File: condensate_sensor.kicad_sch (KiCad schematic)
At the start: 3 parts

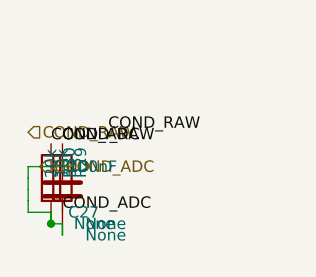
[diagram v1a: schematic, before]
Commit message: fix router map cell no more mark for pins
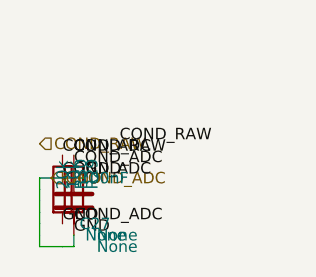
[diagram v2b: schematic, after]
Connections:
- net COND_ADC: now also C27.1

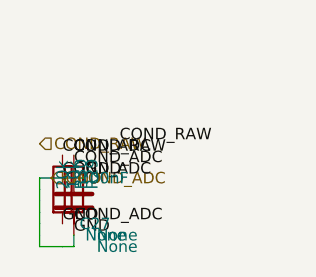
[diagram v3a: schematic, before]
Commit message: исправлены метки
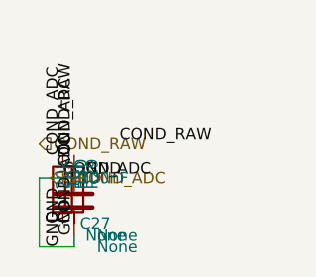
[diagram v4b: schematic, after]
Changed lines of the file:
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@@
 		(instances
 			(project "Untitled"
-				(path "/63851d28-1635-4156-be79-71811504eb15"
+				(path "/a59e5e4e-0756-472a-ad31-66ebbca15e78"
 					(reference "C27")
 					(unit 1)
@@
 		(instances
 			(project "Untitled"
-				(path "/63851d28-1635-4156-be79-71811504eb15"
+				(path "/a59e5e4e-0756-472a-ad31-66ebbca15e78"
 					(reference "R29")
 					(unit 1)
@@
 		(instances
 			(project "Untitled"
-				(path "/63851d28-1635-4156-be79-71811504eb15"
+				(path "/a59e5e4e-0756-472a-ad31-66ebbca15e78"
 					(reference "R30")
 					(unit 1)
@@
 	)
 	(label "GND"
-		(at 15.24 21.59 0)
-		(effects
-			(font
-				(size 1.27 1.27)
-			)
-			(justify left bottom)
-		)
-	)
-	(label "GND"
-		(at 16.51 22.86 0)
-		(effects
-			(font
-				(size 1.27 1.27)
-			)
-			(justify left bottom)
-		)
-	)
-	(label "GND"
-		(at 17.78 16.51 0)
+		(at 15.24 21.59 270)
+		(effects
+			(font
+				(size 1.27 1.27)
+			)
+			(justify left bottom)
+		)
+	)
+	(label "GND"
+		(at 16.51 22.86 270)
+		(effects
+			(font
+				(size 1.27 1.27)
+			)
+			(justify left bottom)
+		)
+	)
+	(label "GND"
+		(at 17.78 16.51 180)
+		(effects
+			(font
+				(size 1.27 1.27)
+			)
+			(justify left bottom)
+		)
+	)
+	(label "GND"
+		(at 15.24 24.13 270)
 		(effects
 			(font
@@
 	)
 	(label "COND_RAW"
-		(at 16.51 13.97 0)
+		(at 16.51 13.97 90)
 		(effects
 			(font
@@
 	)
 	(label "COND_RAW"
-		(at 21.59 12.7 0)
-		(effects
-			(font
-				(size 1.27 1.27)
-			)
-			(justify left bottom)
-		)
-	)
-	(label "COND_ADC"
-		(at 15.24 13.97 0)
-		(effects
-			(font
-				(size 1.27 1.27)
-			)
-			(justify left bottom)
-		)
-	)
-	(label "COND_ADC"
-		(at 16.51 15.24 0)
-		(effects
-			(font
-				(size 1.27 1.27)
-			)
-			(justify left bottom)
-		)
-	)
-	(label "COND_ADC"
-		(at 15.24 16.51 0)
-		(effects
-			(font
-				(size 1.27 1.27)
-			)
-			(justify left bottom)
-		)
-	)
-	(label "COND_ADC"
-		(at 16.51 21.59 0)
-		(effects
-			(font
+		(at 21.59 12.7 180)
+		(effects
+			(font
+				(size 1.27 1.27)
+			)
+			(justify left bottom)
+		)
+	)
+	(label "COND_ADC"
+		(at 15.24 13.97 90)
+		(effects
+			(font
+				(size 1.27 1.27)
+			)
+			(justify left bottom)
+		)
+	)
+	(label "COND_ADC"
+		(at 16.51 15.24 90)
+		(effects
+			(font
+				(size 1.27 1.27)
+			)
+			(justify left bottom)
+		)
+	)
+	(label "COND_ADC"
+		(at 15.24 16.51 0.0000)
+		(effects
+			(font
+				(size 1.27 1.27)
+			)
+			(justify left bottom)
+		)
+	)
+	(label "COND_ADC"
+		(at 16.51 21.59 270)
+		(effects
+			(font

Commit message: fix writer
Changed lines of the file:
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@@
 		(instances
 			(project "Untitled"
-				(path "/a59e5e4e-0756-472a-ad31-66ebbca15e78"
+				(path "/7f9dfed3-5cce-4152-9ab6-c9be91e704d9"
 					(reference "C27")
 					(unit 1)
@@
 		(instances
 			(project "Untitled"
-				(path "/a59e5e4e-0756-472a-ad31-66ebbca15e78"
+				(path "/7f9dfed3-5cce-4152-9ab6-c9be91e704d9"
 					(reference "R29")
 					(unit 1)
@@
 		(instances
 			(project "Untitled"
-				(path "/a59e5e4e-0756-472a-ad31-66ebbca15e78"
+				(path "/7f9dfed3-5cce-4152-9ab6-c9be91e704d9"
 					(reference "R30")
 					(unit 1)
@@
 	(wire
 		(pts
-			(xy 16.51 24.13) (xy 15.24 24.13)
-		)
-		(stroke
-			(width 0)
-			(type default)
-		)
-	)
-	(wire
-		(pts
-			(xy 15.24 24.13) (xy 13.97 24.13)
-		)
-		(stroke
-			(width 0)
-			(type default)
-		)
-	)
-	(wire
-		(pts
-			(xy 13.97 24.13) (xy 12.7 24.13)
-		)
-		(stroke
-			(width 0)
-			(type default)
-		)
-	)
-	(wire
-		(pts
-			(xy 12.7 24.13) (xy 12.7 22.86)
-		)
-		(stroke
-			(width 0)
-			(type default)
-		)
-	)
-	(wire
-		(pts
-			(xy 12.7 22.86) (xy 12.7 21.59)
-		)
-		(stroke
-			(width 0)
-			(type default)
-		)
-	)
-	(wire
-		(pts
-			(xy 12.7 21.59) (xy 12.7 20.32)
-		)
-		(stroke
-			(width 0)
-			(type default)
-		)
-	)
-	(wire
-		(pts
-			(xy 12.7 20.32) (xy 12.7 19.05)
-		)
-		(stroke
-			(width 0)
-			(type default)
-		)
-	)
-	(wire
-		(pts
-			(xy 12.7 19.05) (xy 12.7 17.78)
-		)
-		(stroke
-			(width 0)
-			(type default)
-		)
-	)
-	(wire
-		(pts
-			(xy 12.7 17.78) (xy 12.7 16.51)
+			(xy 16.51 24.13) (xy 12.7 24.13)
+		)
+		(stroke
+			(width 0)
+			(type default)
+		)
+	)
+	(wire
+		(pts
+			(xy 12.7 24.13) (xy 12.7 16.51)
 		)
 		(stroke
@@
 	(hierarchical_label "GND"
 		(shape input)
-		(at 13.97 16.51 180)
+		(at 17.78 16.51 180)
 		(effects
 			(font
@@
 	(hierarchical_label "COND_RAW"
 		(shape input)
-		(at 12.7 12.7 180)
-		(effects
-			(font
+		(at 21.59 12.7 180)
+		(effects
+			(font

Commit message: fic placer for small schemes
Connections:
- net COND_ADC: no longer C27.2, R30.2
- new net GND: C27.2, R30.2
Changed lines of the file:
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@@
 	(symbol
 		(lib_id "Device:C")
-		(at 16.51 19.05 0)
+		(at 16.51 15.24 0)
 		(unit 1)
 		(exclude_from_sim no)
@@
 		(fields_autoplaced no)
 		(property "Reference" "C27"
-			(at 17.145 21.59 0.0000)
+			(at 17.145 17.78 0.0000)
 			(effects
 				(font
@@
 		)
 		(property "Value" "100nF"
-			(at 17.145 16.51 0.0000)
+			(at 17.145 12.7 0.0000)
 			(effects
 				(font
@@
 		)
 		(property "mirror" "None"
-			(at 19.05 24.1299 0)
+			(at 19.05 20.3199 0)
 			(effects
 				(font
@@
 		(instances
 			(project "Untitled"
-				(path "/aeae88a2-db2d-48e3-a72d-65ba09dff43f"
+				(path "/6ad2648c-8bf5-446b-ae62-81d18f8efea8"
 					(reference "C27")
 					(unit 1)
@@
 	(symbol
 		(lib_id "Device:R")
-		(at 16.51 17.78 0)
+		(at 20.32 15.24 0)
 		(unit 1)
 		(exclude_from_sim no)
@@
 		(fields_autoplaced no)
 		(property "Reference" "R29"
-			(at 18.542 17.78 90)
+			(at 22.352 15.24 90)
 			(effects
 				(font
@@
 		)
 		(property "Value" "10k"
-			(at 16.51 17.78 90)
+			(at 20.32 15.24 90)
 			(effects
 				(font
@@
 		)
 		(property "mirror" "None"
-			(at 19.05 22.8599 0)
+			(at 22.86 20.3199 0)
 			(effects
 				(font
@@
 		(instances
 			(project "Untitled"
-				(path "/aeae88a2-db2d-48e3-a72d-65ba09dff43f"
+				(path "/6ad2648c-8bf5-446b-ae62-81d18f8efea8"
 					(reference "R29")
 					(unit 1)
@@
 	(symbol
 		(lib_id "Device:R")
-		(at 15.24 17.78 0)
+		(at 12.7 15.24 0)
 		(unit 1)
 		(exclude_from_sim no)
@@
 		(fields_autoplaced no)
 		(property "Reference" "R30"
-			(at 17.272 17.78 90)
+			(at 14.732 15.24 90)
 			(effects
 				(font
@@
 		)
 		(property "Value" "20k"
-			(at 15.24 17.78 90)
+			(at 12.7 15.24 90)
 			(effects
 				(font
@@
 		)
 		(property "mirror" "None"
-			(at 17.78 22.8599 0)
+			(at 15.24 20.3199 0)
 			(effects
 				(font
@@
 		(instances
 			(project "Untitled"
-				(path "/aeae88a2-db2d-48e3-a72d-65ba09dff43f"
+				(path "/6ad2648c-8bf5-446b-ae62-81d18f8efea8"
 					(reference "R30")
 					(unit 1)
@@
 	(wire
 		(pts
-			(xy 16.51 22.86) (xy 16.51 24.13)
-		)
-		(stroke
-			(width 0)
-			(type default)
-		)
-	)
-	(wire
-		(pts
-			(xy 16.51 24.13) (xy 12.7 24.13)
-		)
-		(stroke
-			(width 0)
-			(type default)
-		)
-	)
-	(wire
-		(pts
-			(xy 12.7 24.13) (xy 12.7 16.51)
-		)
-		(stroke
-			(width 0)
-			(type default)
-		)
-	)
-	(wire
-		(pts
-			(xy 12.7 16.51) (xy 17.78 16.51)
-		)
-		(stroke
-			(width 0)
-			(type default)
-		)
+			(xy 12.7 11.43) (xy 12.7 10.16)
+		)
+		(stroke
+			(width 0)
+			(type default)
+		)
+	)
+	(wire
+		(pts
+			(xy 12.7 10.16) (xy 16.51 10.16)
+		)
+		(stroke
+			(width 0)
+			(type default)
+		)
+	)
+	(wire
+		(pts
+			(xy 16.51 10.16) (xy 16.51 11.43)
+		)
+		(stroke
+			(width 0)
+			(type default)
+		)
+	)
+	(wire
+		(pts
+			(xy 16.51 20.32) (xy 26.67 20.32)
+		)
+		(stroke
+			(width 0)
+			(type default)
+		)
+	)
+	(wire
+		(pts
+			(xy 26.67 20.32) (xy 29.21 20.32)
+		)
+		(stroke
+			(width 0)
+			(type default)
+		)
+	)
+	(wire
+		(pts
+			(xy 29.21 20.32) (xy 29.21 7.62)
+		)
+		(stroke
+			(width 0)
+			(type default)
+		)
+	)
+	(wire
+		(pts
+			(xy 29.21 7.62) (xy 16.51 7.62)
+		)
+		(stroke
+			(width 0)
+			(type default)
+		)
+	)
+	(wire
+		(pts
+			(xy 16.51 7.62) (xy 16.51 10.16)
+		)
+		(stroke
+			(width 0)
+			(type default)
+		)
+	)
+	(junction
+		(at 16.51 10.16)
+		(diameter 0)
+		(color 0 0 0 0)
 	)
 	(label "GND"
-		(at 15.24 21.59 270)
+		(at 16.51 19.05 270)
 		(effects
 			(font
@@
 	)
 	(label "GND"
-		(at 16.51 22.86 270)
+		(at 15.24 20.32 180)
 		(effects
 			(font
@@
 	)
 	(label "GND"
-		(at 17.78 16.51 180)
-		(effects
-			(font
-				(size 1.27 1.27)
-			)
-			(justify left bottom)
-		)
-	)
-	(label "GND"
-		(at 15.24 24.13 270)
+		(at 12.7 19.05 270)
 		(effects
 			(font
@@
 	)
 	(label "COND_RAW"
-		(at 16.51 13.97 90)
+		(at 20.32 11.43 90)
 		(effects
 			(font
@@
 	)
 	(label "COND_RAW"
-		(at 21.59 12.7 180)
+		(at 27.94 8.89 180)
 		(effects
 			(font
@@
 	)
 	(label "COND_ADC"
-		(at 15.24 13.97 90)
+		(at 20.32 19.05 270)
 		(effects
 			(font
@@
 	)
 	(label "COND_ADC"
-		(at 16.51 15.24 90)
-		(effects
-			(font
-				(size 1.27 1.27)
-			)
-			(justify left bottom)
-		)
-	)
-	(label "COND_ADC"
-		(at 15.24 16.51 0.0000)
-		(effects
-			(font
-				(size 1.27 1.27)
-			)
-			(justify left bottom)
-		)
-	)
-	(label "COND_ADC"
-		(at 16.51 21.59 270)
+		(at 16.51 10.16 270)
 		(effects
 			(font
@@
 	(hierarchical_label "GND"
 		(shape input)
-		(at 17.78 16.51 180)
+		(at 15.24 20.32 180)
 		(effects
 			(font
@@
 	(hierarchical_label "COND_RAW"
 		(shape input)
-		(at 21.59 12.7 180)
+		(at 27.94 8.89 180)
 		(effects
 			(font
@@
 	(hierarchical_label "COND_ADC"
 		(shape input)
-		(at 15.24 16.51 0)
-		(effects
-			(font
+		(at 16.51 20.32 0)
+		(effects
+			(font
